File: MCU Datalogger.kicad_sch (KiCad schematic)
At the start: 7 parts

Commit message: add a new resistor
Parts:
- added R5, R6: R, symbol Device:R
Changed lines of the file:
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@@
+	)
+	(symbol
+		(lib_id "Device:R")
+		(at 100.33 73.66 0)
+		(unit 1)
+		(exclude_from_sim no)
+		(in_bom yes)
+		(on_board yes)
+		(dnp no)
+		(fields_autoplaced yes)
+		(property "Reference" "R5"
+			(at 102.87 72.3899 0)
+			(effects
+				(font
+					(size 1.27 1.27)
+				)
+				(justify left)
+			)
+		)
+		(property "Value" "R"
+			(at 102.87 74.9299 0)
+			(effects
+				(font
+					(size 1.27 1.27)
+				)
+				(justify left)
+			)
+		)
+		(property "Footprint" ""
+			(at 98.552 73.66 90)
+			(effects
+				(font
+					(size 1.27 1.27)
+				)
+				(hide yes)
+			)
+		)
+		(property "Datasheet" "~"
+			(at 100.33 73.66 0)
+			(effects
+				(font
+					(size 1.27 1.27)
+				)
+				(hide yes)
+			)
+		)
+		(property "Description" "Resistor"
+			(at 100.33 73.66 0)
+			(effects
+				(font
+					(size 1.27 1.27)
+				)
+				(hide yes)
+			)
+		)
+		(pin "1"
+		)
+		(pin "2"
+		)
+		(instances
+			(project "MCU Datalogger"
+				(path "/2d095fec-de04-4caa-8a5d-d4c981edd86b"
+					(reference "R5")
+					(unit 1)
+				)
+			)
+		)
 	)
 	(symbol
@@
 					(unit 1)
 				)
+			)
+		)
+	)
+	(symbol
+		(lib_id "Device:R")
+		(at 114.1543 75.8198 0)
+		(unit 1)
+		(exclude_from_sim no)
+		(in_bom yes)
+		(on_board yes)
+		(dnp no)
+		(fields_autoplaced yes)
+		(property "Reference" "R6"
+			(at 116.6943 74.5497 0)
+			(effects
+				(font
+					(size 1.27 1.27)
+				)
+				(justify left)
+			)
+		)
+		(property "Value" "R"
+			(at 116.6943 77.0897 0)
+			(effects
+				(font
+					(size 1.27 1.27)
+				)
+				(justify left)
+			)
+		)
+		(property "Footprint" ""
+			(at 112.3763 75.8198 90)
+			(effects
+				(font
+					(size 1.27 1.27)
+				)
+				(hide yes)
+			)
+		)
+		(property "Datasheet" "~"
+			(at 114.1543 75.8198 0)
+			(effects
+				(font
+					(size 1.27 1.27)
+				)
+				(hide yes)
+			)
+		)
+		(property "Description" "Resistor"
+			(at 114.1543 75.8198 0)
+			(effects
+				(font
+					(size 1.27 1.27)
+				)
+				(hide yes)
+			)
+		)
+		(pin "1"
+		)
+		(pin "2"
+		)
+		(instances
+			(project "MCU Datalogger"
+				(path "/2d095fec-de04-4caa-8a5d-d4c981edd86b"
+					(reference "R6")
+					(unit 1)
+				)

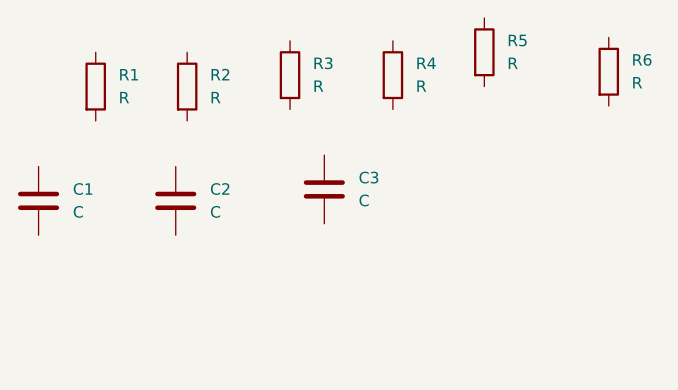
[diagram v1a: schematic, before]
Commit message: new branch with new capacitor
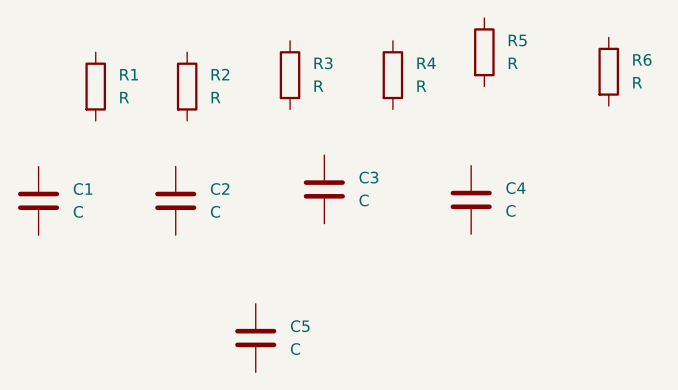
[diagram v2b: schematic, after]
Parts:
- added C4, C5: C, symbol Device:C
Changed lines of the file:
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@@
 	(paper "A4")
+	(symbol
+		(lib_id "Device:C")
+		(at 98.8658 90.0648 0)
+		(unit 1)
+		(exclude_from_sim no)
+		(in_bom yes)
+		(on_board yes)
+		(dnp no)
+		(fields_autoplaced yes)
+		(property "Reference" "C4"
+			(at 102.6758 88.7947 0)
+			(effects
+				(font
+					(size 1.27 1.27)
+				)
+				(justify left)
+			)
+		)
+		(property "Value" "C"
+			(at 102.6758 91.3347 0)
+			(effects
+				(font
+					(size 1.27 1.27)
+				)
+				(justify left)
+			)
+		)
+		(property "Footprint" ""
+			(at 99.831 93.8748 0)
+			(effects
+				(font
+					(size 1.27 1.27)
+				)
+				(hide yes)
+			)
+		)
+		(property "Datasheet" "~"
+			(at 98.8658 90.0648 0)
+			(effects
+				(font
+					(size 1.27 1.27)
+				)
+				(hide yes)
+			)
+		)
+		(property "Description" "Unpolarized capacitor"
+			(at 98.8658 90.0648 0)
+			(effects
+				(font
+					(size 1.27 1.27)
+				)
+				(hide yes)
+			)
+		)
+		(pin "1"
+		)
+		(pin "2"
+		)
+		(instances
+			(project "MCU Datalogger"
+				(path "/2d095fec-de04-4caa-8a5d-d4c981edd86b"
+					(reference "C4")
+					(unit 1)
+				)
+			)
+		)
+	)
+	(symbol
+		(lib_id "Device:C")
+		(at 74.93 105.41 0)
+		(unit 1)
+		(exclude_from_sim no)
+		(in_bom yes)
+		(on_board yes)
+		(dnp no)
+		(fields_autoplaced yes)
+		(property "Reference" "C5"
+			(at 78.74 104.1399 0)
+			(effects
+				(font
+					(size 1.27 1.27)
+				)
+				(justify left)
+			)
+		)
+		(property "Value" "C"
+			(at 78.74 106.6799 0)
+			(effects
+				(font
+					(size 1.27 1.27)
+				)
+				(justify left)
+			)
+		)
+		(property "Footprint" ""
+			(at 75.8952 109.22 0)
+			(effects
+				(font
+					(size 1.27 1.27)
+				)
+				(hide yes)
+			)
+		)
+		(property "Datasheet" "~"
+			(at 74.93 105.41 0)
+			(effects
+				(font
+					(size 1.27 1.27)
+				)
+				(hide yes)
+			)
+		)
+		(property "Description" "Unpolarized capacitor"
+			(at 74.93 105.41 0)
+			(effects
+				(font
+					(size 1.27 1.27)
+				)
+				(hide yes)
+			)
+		)
+		(pin "1"
+		)
+		(pin "2"
+		)
+		(instances
+			(project "MCU Datalogger"
+				(path "/2d095fec-de04-4caa-8a5d-d4c981edd86b"
+					(reference "C5")
+					(unit 1)
+				)
+			)
+		)
+	)
 	(symbol
 		(lib_id "Device:R")

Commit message: edited a few resistors
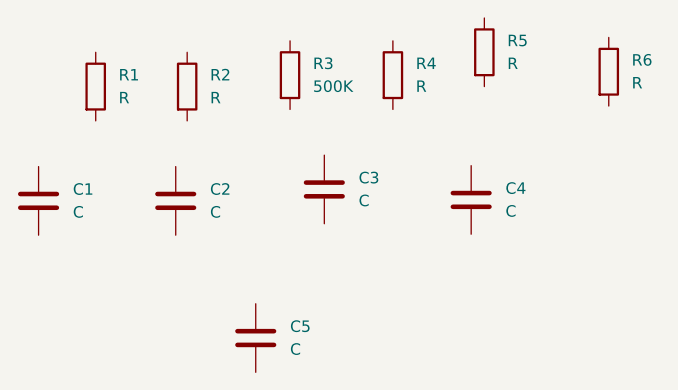
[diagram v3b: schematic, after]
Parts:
- R3: value R -> 500K
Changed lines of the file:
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@@
 			)
 		)
-		(property "Value" "R"
+		(property "Value" "500K"
 			(at 81.28 77.4699 0)
 			(effects
@@
 			(at 78.74 76.2 0)
 			(effects
+				(font
+					(size 1.27 1.27)
+				)
+				(hide yes)
+			)
+		)
+		(property "descrisc" ""
+			(at 78.74 76.2 0)
+			(effects
